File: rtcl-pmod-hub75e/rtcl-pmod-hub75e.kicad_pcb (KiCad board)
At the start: 4 copper layers, 20 x 56 mm, 22 parts, among them J1 PMOD, J2 HIF3FC-16PA-2.54DSA(71), J3 Conn_01x02, U1 74LVC273, U2 74LVC273, U3 74LVC273, U4 74LVC273, U5 LM809M3-2.93, U6 74LVC2G86

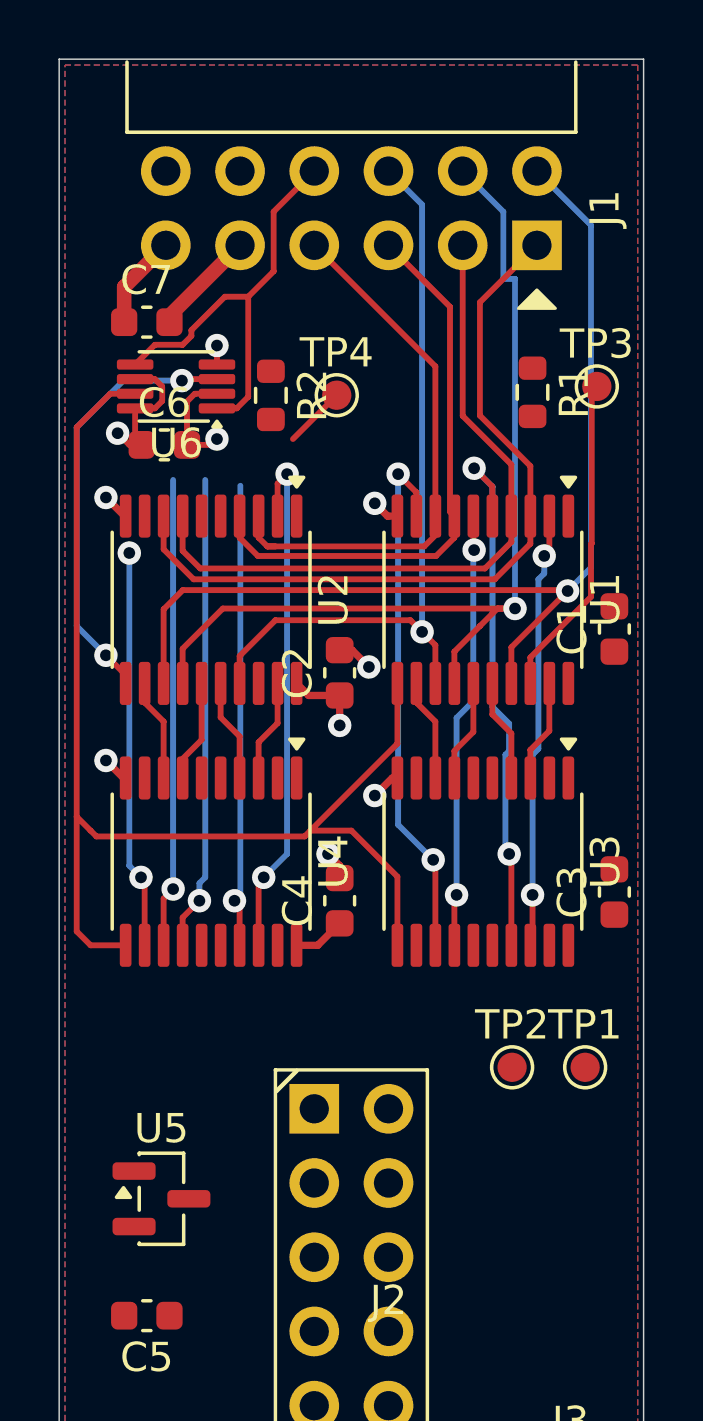
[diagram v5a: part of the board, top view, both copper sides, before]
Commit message: Update active layer and adjust wire positions in schematic
- Changed active layer from 0 to 2 in the PCB layout.
- Adjusted multiple wire coordinates in the schematic to correct alignment.
- Updated label positions for various components to ensure proper placement.
- Modified test point coordinates for better alignment with the design.
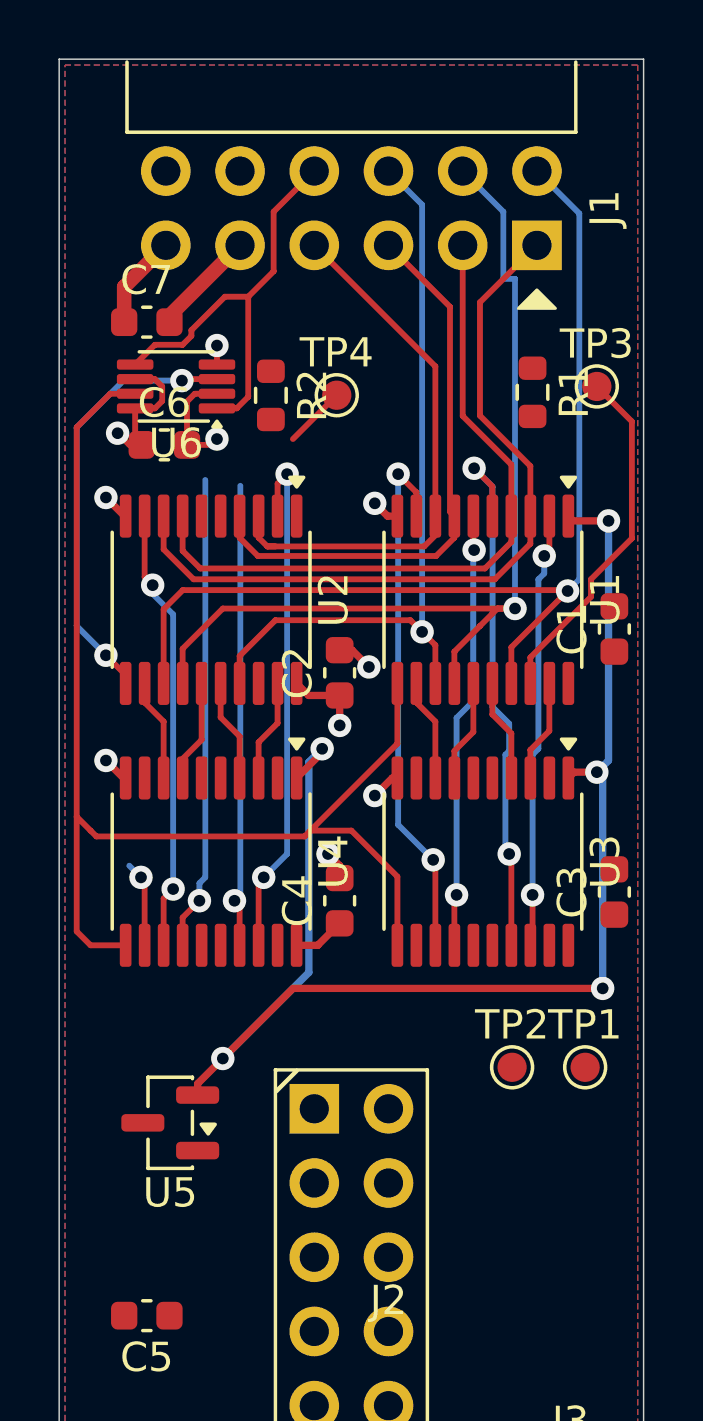
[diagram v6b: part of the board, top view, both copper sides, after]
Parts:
- moved U5 2.62 mm to (103.8, 86.4), turned to 180 degrees
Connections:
- TP1 pad 1: Net-(U3-Q7) -> Net-(U3-Q0)
- TP2 pad 1: Net-(U4-Q7) -> Net-(U4-Q0)
- U2 pad 2: /D0N -> /D3N
- U2 pad 5: /D1N -> /D2N
- U2 pad 6: /D2N -> /D1N
- U2 pad 9: /D3N -> /D0N
- U3 pad 12: /HUB75_B -> /HUB75_A
- U3 pad 15: /HUB75_C -> /HUB75_CKE
- U3 pad 16: /HUB75_D -> /HUB75_LAT
- U3 pad 19: Net-(U3-Q7) -> /HUB75_OE
- U3 pad 2: /HUB75_OE -> Net-(U3-Q0)
- U3 pad 5: /HUB75_LAT -> /HUB75_B
- U3 pad 6: /HUB75_CKE -> /HUB75_C
- U3 pad 9: /HUB75_A -> /HUB75_D
- U4 pad 12: /HUB75_R2 -> /HUB75_E
- U4 pad 13: /D3N -> /D0N
- U4 pad 14: /D2N -> /D1N
- U4 pad 15: /HUB75_G2 -> /HUB75_R1
- U4 pad 16: /HUB75_B2 -> /HUB75_G1
- U4 pad 17: /D1N -> /D2N
- U4 pad 18: /D0N -> /D3N
- U4 pad 19: Net-(U4-Q7) -> /HUB75_B1
- U4 pad 2: /HUB75_E -> Net-(U4-Q0)
- U4 pad 5: /HUB75_R1 -> /HUB75_B2
- U4 pad 6: /HUB75_G1 -> /HUB75_G2
- U4 pad 9: /HUB75_B1 -> /HUB75_R2
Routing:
- net /RESET: track 0.00 -> 47.7 mm, vias 0 -> 5
- net /HUB75_R2: track 13.9 -> 0.00 mm, vias 2 -> 0
- net /HUB75_E: track 0.00 -> 2.94 mm, vias 0 -> 1
- net /D0N: track 18.1 -> 15.2 mm
- net /D3N: track 16.1 -> 18.1 mm, vias 1 -> 2
- net Net-(U1-D7): track 11.1 -> 12.1 mm

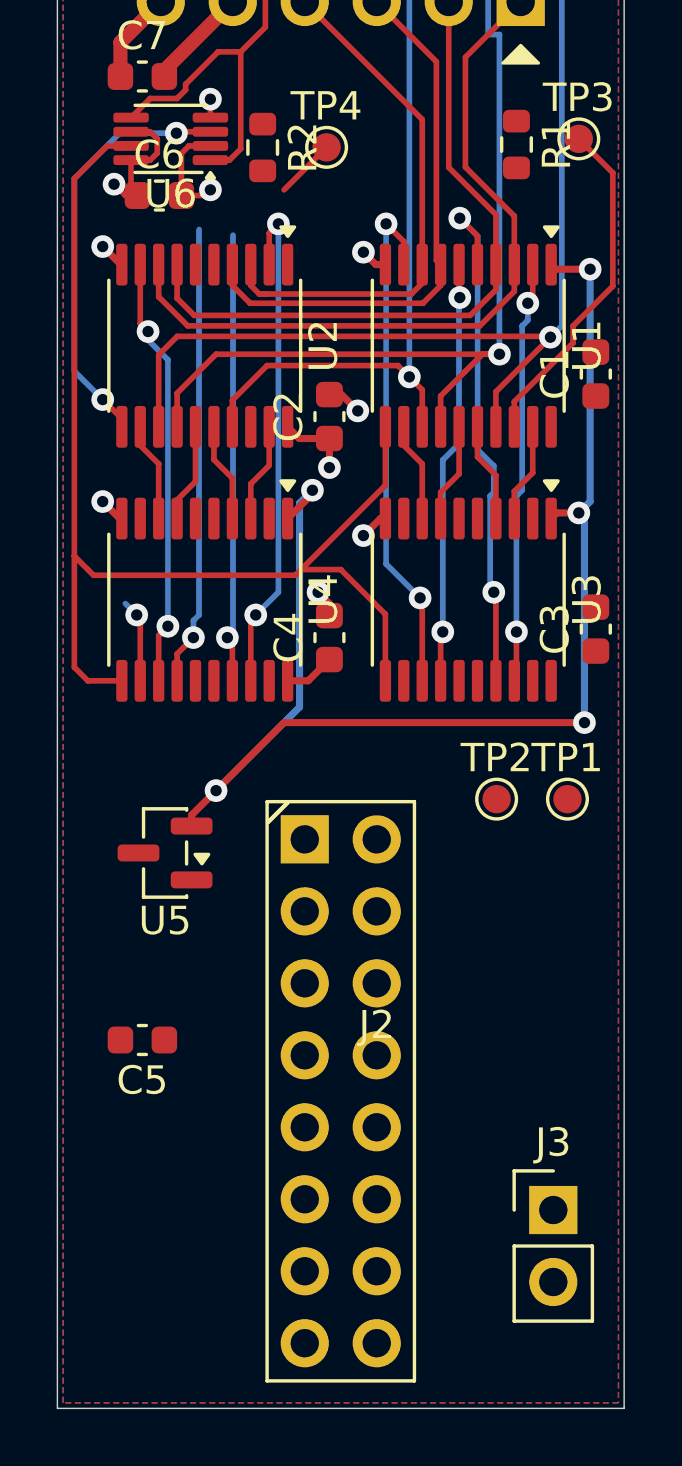
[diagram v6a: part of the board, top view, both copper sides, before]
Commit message: Update selection filter and zone display mode in KiCad project file
- Changed selection filter for footprints from true to false
- Updated zone display mode from 0 to 1
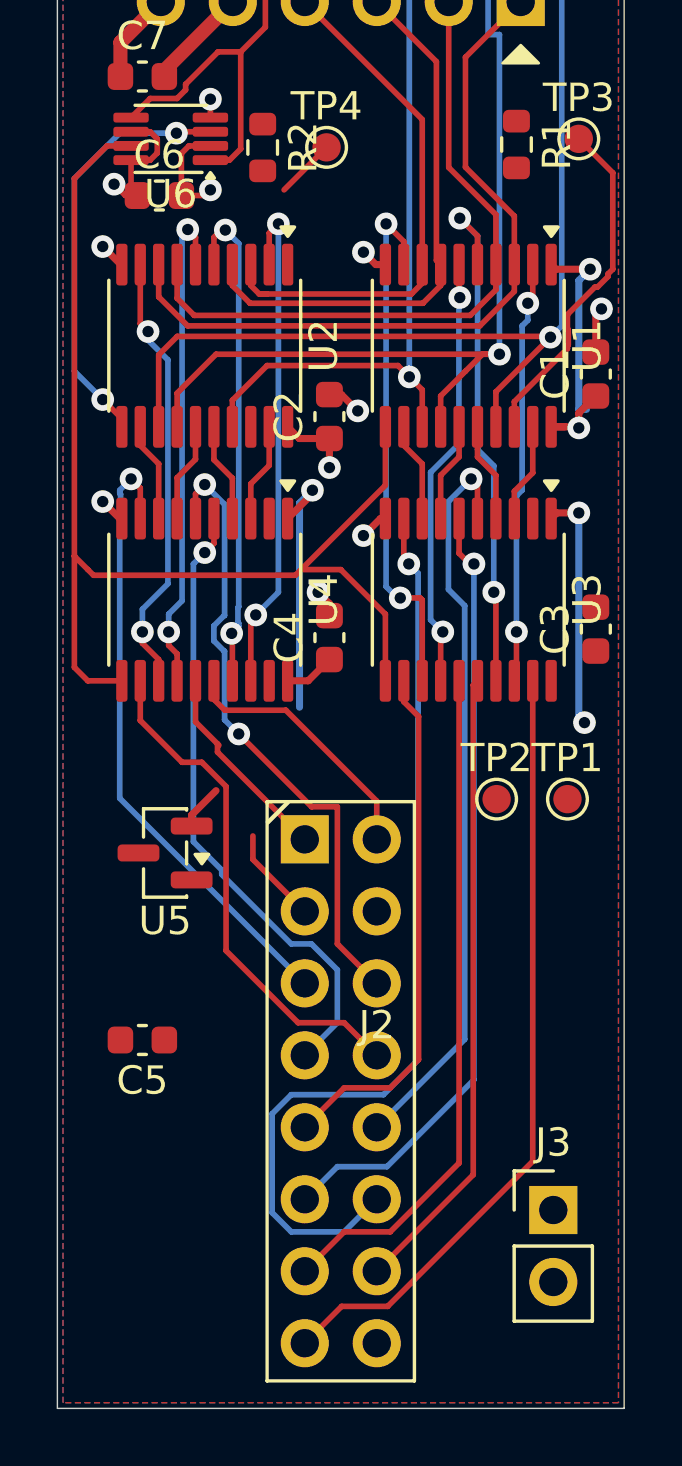
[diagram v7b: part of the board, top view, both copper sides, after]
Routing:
- net /HUB75_D: track 0.00 -> 33.2 mm, vias 0 -> 1
- net /HUB75_C: track 0.00 -> 27.9 mm, vias 0 -> 1
- net /HUB75_OE: track 0.00 -> 27.7 mm
- net /HUB75_B: track 0.00 -> 26.2 mm, vias 0 -> 1
- net /HUB75_CKE: track 0.00 -> 24.0 mm
- net /HUB75_G2: track 0.00 -> 22.3 mm, vias 0 -> 2
- net /HUB75_LAT: track 0.00 -> 22.3 mm
- net /HUB75_B2: track 0.00 -> 22.2 mm, vias 0 -> 1
- net /HUB75_R2: track 0.00 -> 22.2 mm, vias 0 -> 1
- net /RESET: track 47.7 -> 26.5 mm, vias 5 -> 4
- net /HUB75_A: track 0.00 -> 18.6 mm
- net /HUB75_E: track 2.94 -> 18.0 mm, vias 1 -> 0
- net /HUB75_G1: track 0.00 -> 9.24 mm
- net /HUB75_R1: track 0.00 -> 7.26 mm
- net /HUB75_B1: track 0.00 -> 3.42 mm
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
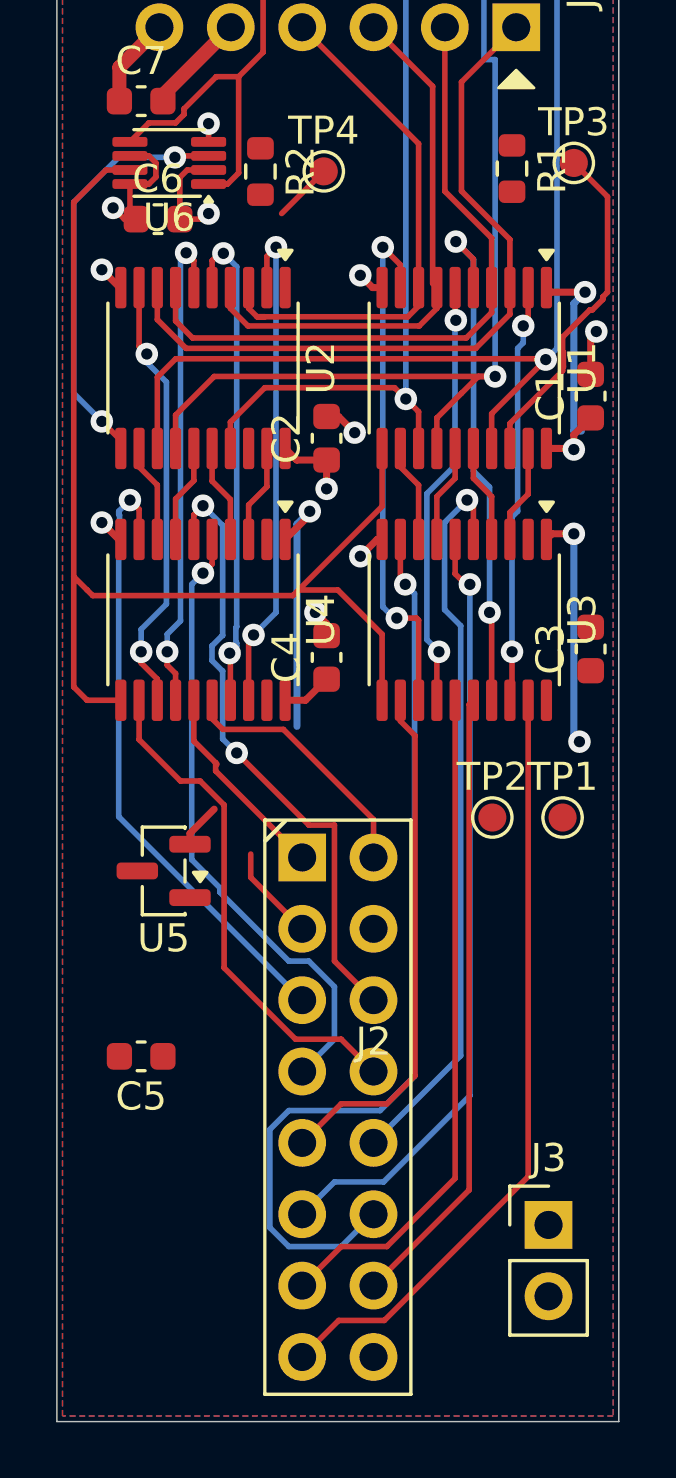
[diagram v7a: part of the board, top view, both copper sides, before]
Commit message: Disable vias visibility in the PCB layout for the rtcl-pmod-hub75e project
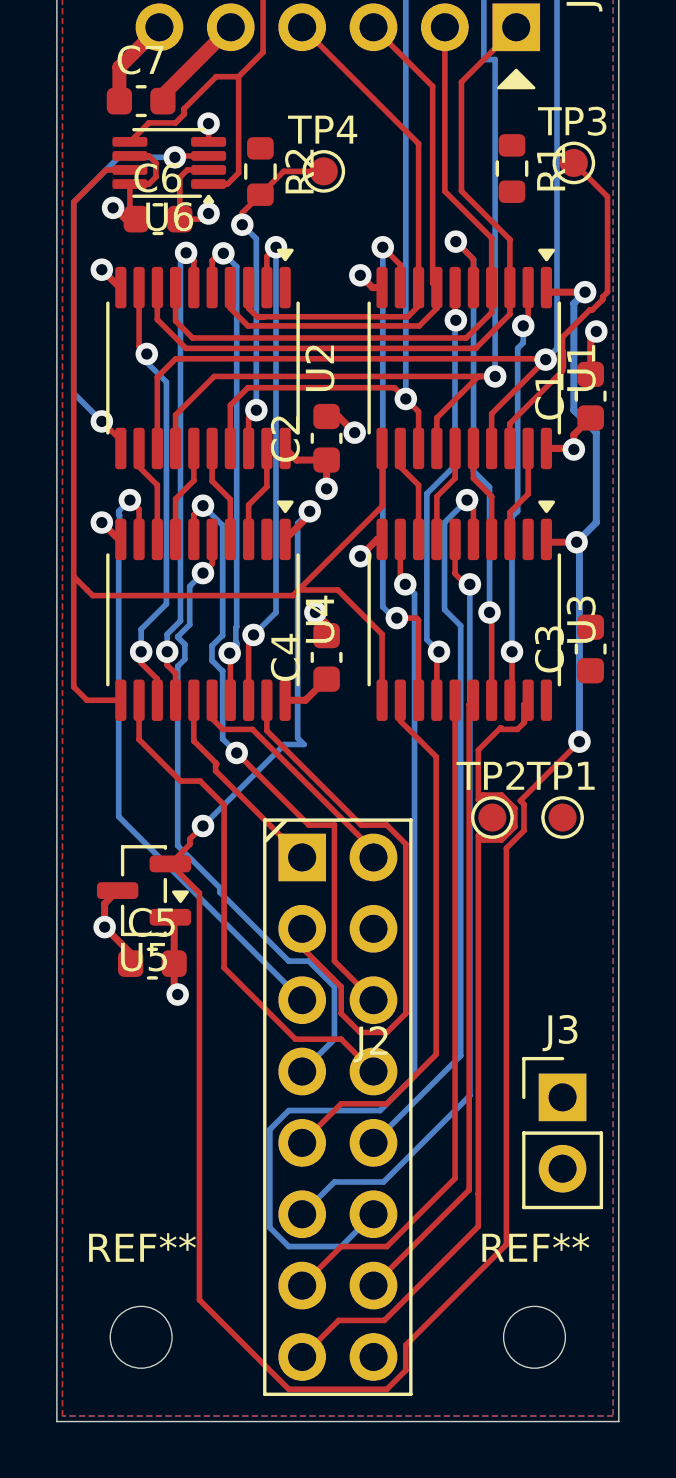
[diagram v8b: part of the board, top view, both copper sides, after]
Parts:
- added REF**: MountingHole_2.2mm_M2, MountingHole:MountingHole_2.2mm_M2, F.Cu at (103.0, 103.0)
- added REF**: MountingHole_2.2mm_M2, MountingHole:MountingHole_2.2mm_M2, F.Cu at (117.0, 103.0)
- moved J3 4.57 mm to (118.0, 94.5)
- moved C5 3.32 mm to (103.4, 89.7), turned to 0 degrees
- moved U5 0.99 mm to (103.1, 87.1)
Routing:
- net /RESET: track 26.5 -> 86.2 mm, vias 4 -> 5
- net /HUB75_B1: track 3.42 -> 20.2 mm
- net Net-(U2-D7): track 2.12 -> 12.2 mm, vias 0 -> 2
- net +3.3V: track 15.4 -> 18.6 mm, vias 3 -> 4
- net /HUB75_OE: track 27.7 -> 30.6 mm
- net GND: track 15.7 -> 18.5 mm, vias 9 -> 10
- net /HUB75_G1: track 9.24 -> 8.59 mm
- net /HUB75_B2: track 22.2 -> 22.9 mm
- net /HUB75_A: track 18.6 -> 19.2 mm
